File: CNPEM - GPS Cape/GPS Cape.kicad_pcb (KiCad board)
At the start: 2 copper layers, 11 parts, among them J101 Adafruit_ultimate_GPS_breakout, U101 74LS123

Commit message: schematics and pcb finished
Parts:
- added C104: 100n, Capacitors_SMD:C_0805_HandSoldering, F.Cu at (172.1, 94.0)
- added C105: 100n, Capacitors_SMD:C_0805_HandSoldering, F.Cu at (143.5, 99.1)
- added C106: 0.1u, Capacitors_SMD:C_0805_HandSoldering, B.Cu at (132.7, 96.5)
- added R103: 10k, Resistors_SMD:R_0805_HandSoldering, F.Cu at (149.9, 116.2)
- added R104: 10k, Resistors_SMD:R_0805_HandSoldering, B.Cu at (132.7, 101.0)
- moved D101 10.5 mm to (144.8, 116.2), turned to 270 degrees
- moved C103 8.98 mm to (151.8, 111.1)
- moved JP102 8.89 mm to (164.5, 87.0)
- moved JP101 8.25 mm to (159.4, 87.0)
- moved R102 6.35 mm to (147.3, 105.4), turned to 90 degrees
- moved C102 3.42 mm to (154.9, 116.2)
- moved C101 2.54 mm to (151.8, 99.1), turned to 0 degrees
- moved R101 1.80 mm to (154.9, 105.4)
- moved Beagle101 0.25 mm to (148.6, 104.8)
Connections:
- Beagle101 pad B1: (no net) -> GND
- Beagle101 pad B10: (no net) -> Net-(Beagle101-PadB10)
- Beagle101 pad B11: (no net) -> Net-(Beagle101-PadB11)
- Beagle101 pad B12: (no net) -> Net-(Beagle101-PadB12)
- Beagle101 pad B13: (no net) -> Net-(Beagle101-PadB13)
- Beagle101 pad B14: (no net) -> Net-(Beagle101-PadB14)
- Beagle101 pad B15: (no net) -> Net-(Beagle101-PadB15)
- Beagle101 pad B16: (no net) -> Net-(Beagle101-PadB16)
- Beagle101 pad B17: (no net) -> Net-(Beagle101-PadB17)
- Beagle101 pad B18: (no net) -> Net-(Beagle101-PadB18)
- Beagle101 pad B19: (no net) -> Net-(Beagle101-PadB19)
- Beagle101 pad B2: (no net) -> Net-(Beagle101-PadB2)
- Beagle101 pad B20: (no net) -> Net-(Beagle101-PadB20)
- Beagle101 pad B21: (no net) -> Net-(Beagle101-PadB21)
- Beagle101 pad B22: (no net) -> Net-(Beagle101-PadB22)
- Beagle101 pad B23: (no net) -> Net-(Beagle101-PadB23)
- Beagle101 pad B24: (no net) -> Net-(Beagle101-PadB24)
- Beagle101 pad B25: (no net) -> Net-(Beagle101-PadB25)
- Beagle101 pad B26: (no net) -> Net-(Beagle101-PadB26)
- Beagle101 pad B27: (no net) -> Net-(Beagle101-PadB27)
- Beagle101 pad B28: (no net) -> Net-(Beagle101-PadB28)
- Beagle101 pad B29: (no net) -> Net-(Beagle101-PadB29)
- Beagle101 pad B3: (no net) -> Net-(Beagle101-PadB3)
- Beagle101 pad B30: (no net) -> Net-(Beagle101-PadB30)
- Beagle101 pad B31: (no net) -> Net-(Beagle101-PadB31)
- Beagle101 pad B32: (no net) -> Net-(Beagle101-PadB32)
- Beagle101 pad B33: (no net) -> Net-(Beagle101-PadB33)
- Beagle101 pad B34: (no net) -> Net-(Beagle101-PadB34)
- Beagle101 pad B35: (no net) -> Net-(Beagle101-PadB35)
- Beagle101 pad B36: (no net) -> Net-(Beagle101-PadB36)
- Beagle101 pad B37: (no net) -> Net-(Beagle101-PadB37)
- Beagle101 pad B38: (no net) -> Net-(Beagle101-PadB38)
- Beagle101 pad B39: (no net) -> Net-(Beagle101-PadB39)
- Beagle101 pad B4: (no net) -> Net-(Beagle101-PadB4)
- Beagle101 pad B40: (no net) -> Net-(Beagle101-PadB40)
- Beagle101 pad B41: (no net) -> Net-(Beagle101-PadB41)
- Beagle101 pad B42: (no net) -> Net-(Beagle101-PadB42)
- Beagle101 pad B43: (no net) -> Net-(Beagle101-PadB43)
- Beagle101 pad B44: (no net) -> Net-(Beagle101-PadB44)
- Beagle101 pad B45: (no net) -> Net-(Beagle101-PadB45)
- Beagle101 pad B46: (no net) -> Net-(Beagle101-PadB46)
- Beagle101 pad B5: (no net) -> Net-(Beagle101-PadB5)
- Beagle101 pad B6: (no net) -> Net-(Beagle101-PadB6)
- Beagle101 pad B7: (no net) -> Net-(Beagle101-PadB7)
- Beagle101 pad B8: (no net) -> Net-(Beagle101-PadB8)
- Beagle101 pad B9: (no net) -> Net-(Beagle101-PadB9)
- Beagle101 pad C4: +3V3 -> VCC
- Beagle101 pad C44: Net-(Beagle101-PadC44) -> GND
- C102 pad 2: +3V3 -> Net-(C102-Pad2)
- D101 pad 2: +3V3 -> VCC
- J101 pad 2: +3V3 -> Net-(C106-Pad2)
- J101 pad 8: +3V3 -> VCC
- R101 pad 1: +3V3 -> VCC
- U101 pad 16: +3V3 -> VCC
- U101 pad 3: +3V3 -> Net-(C102-Pad2)
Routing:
- net VCC: track 0.00 -> 97.4 mm
- net +3V3: track 47.1 -> 0.00 mm
- net /TX_GPS: track 0.00 -> 36.4 mm
- net GND: track 95.2 -> 128.3 mm
- net /RX_GPS: track 0.00 -> 32.9 mm
- net Net-(C101-Pad1): track 5.47 -> 32.1 mm
- net Net-(C102-Pad2): track 0.00 -> 22.0 mm
- net Net-(C106-Pad2): track 0.00 -> 19.7 mm
- net /PPS_ENL: track 28.8 -> 18.6 mm
- net Net-(C103-Pad1): track 8.08 -> 16.1 mm
- net Net-(D101-Pad1): track 3.32 -> 9.45 mm
- net /PPS: track 30.2 -> 35.6 mm
- net Net-(Beagle101-PadC12): track 10.8 -> 10.2 mm
- added copper zone on B.Cu, net GND
- added copper zone on F.Cu, net GND
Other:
- board outline added: 87 x 54.6 mm

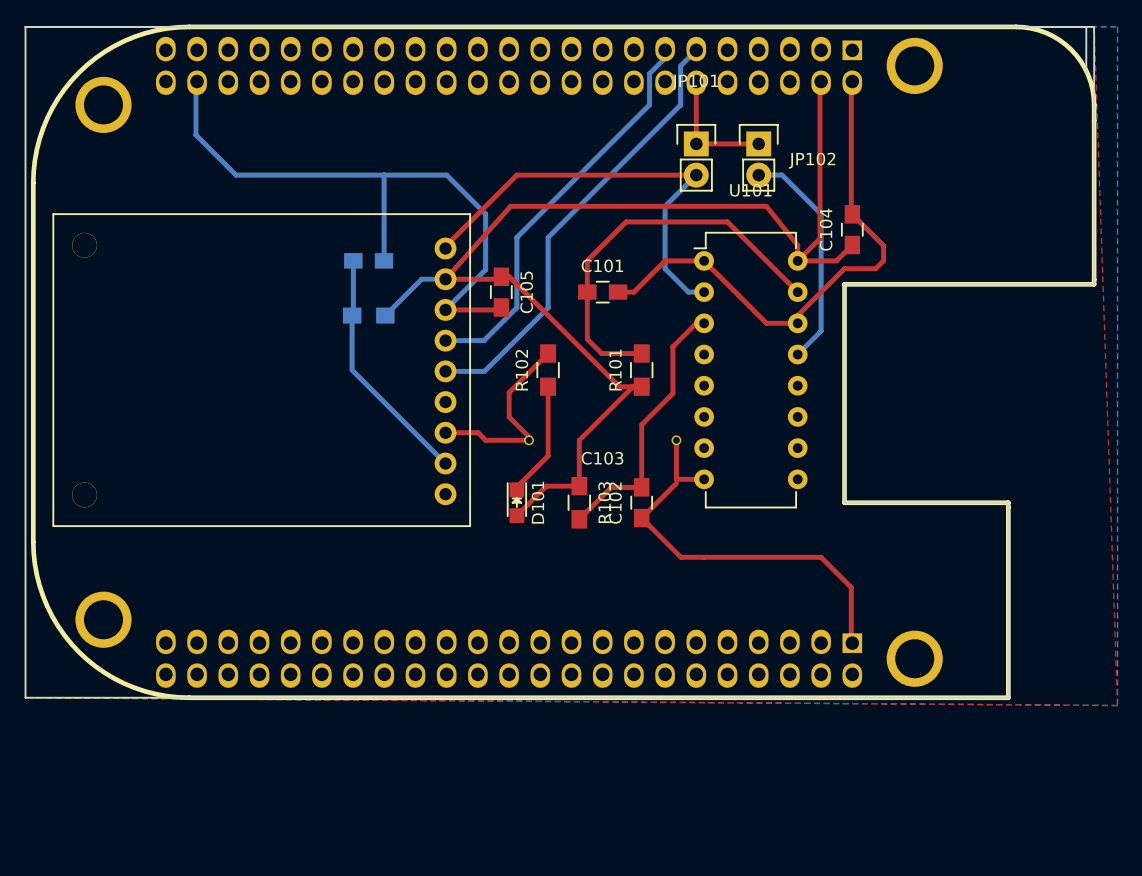
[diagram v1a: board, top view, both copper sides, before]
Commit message: bbb pins connections put in bottom layer and logo inserted
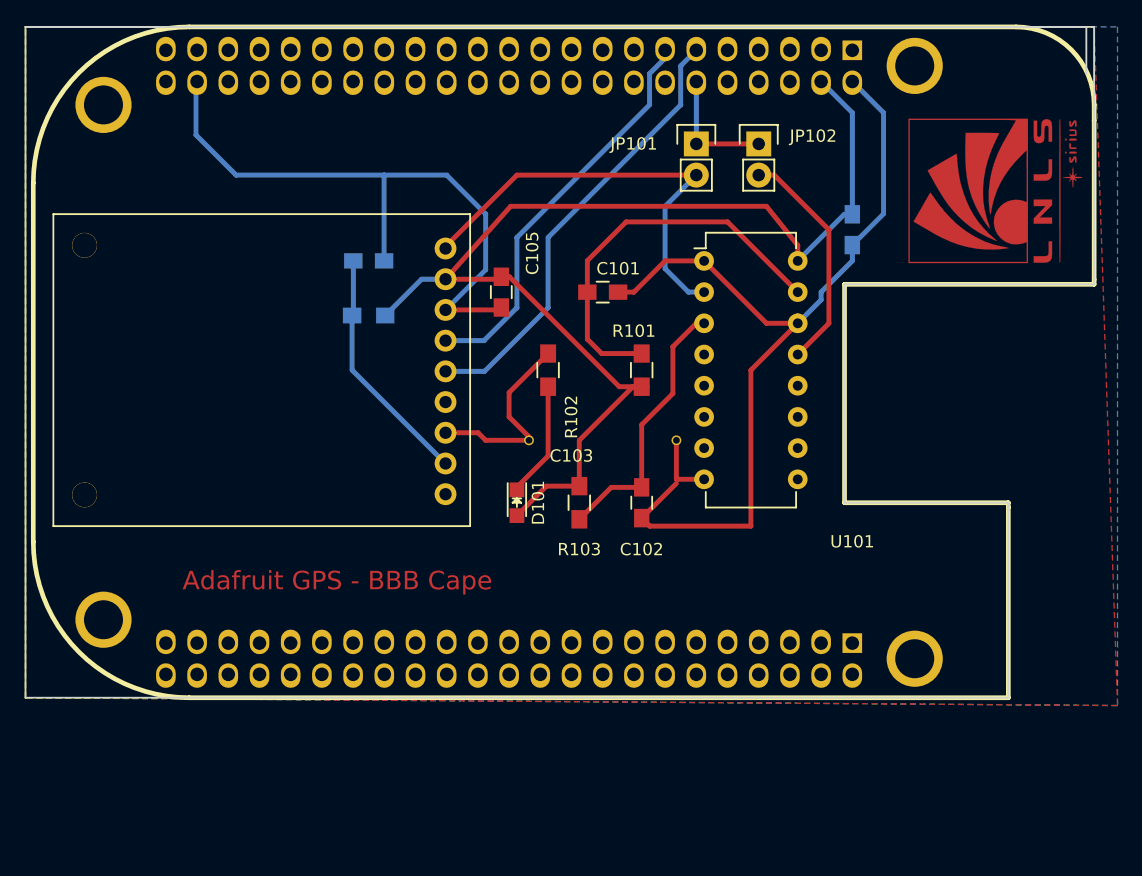
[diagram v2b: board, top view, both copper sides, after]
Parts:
- added G***: LOGO, Controle:LNLS_Conversor_USB_RS485, F.Cu at (183.5, 90.8)
- C104: moved to B.Cu
- turned C104 to 270 degrees
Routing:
- net GND: track 128.3 -> 130.7 mm
- net VCC: track 97.4 -> 95.8 mm
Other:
- board text added: "Adafruit GPS - BBB Cape"

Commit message: LED and components revised
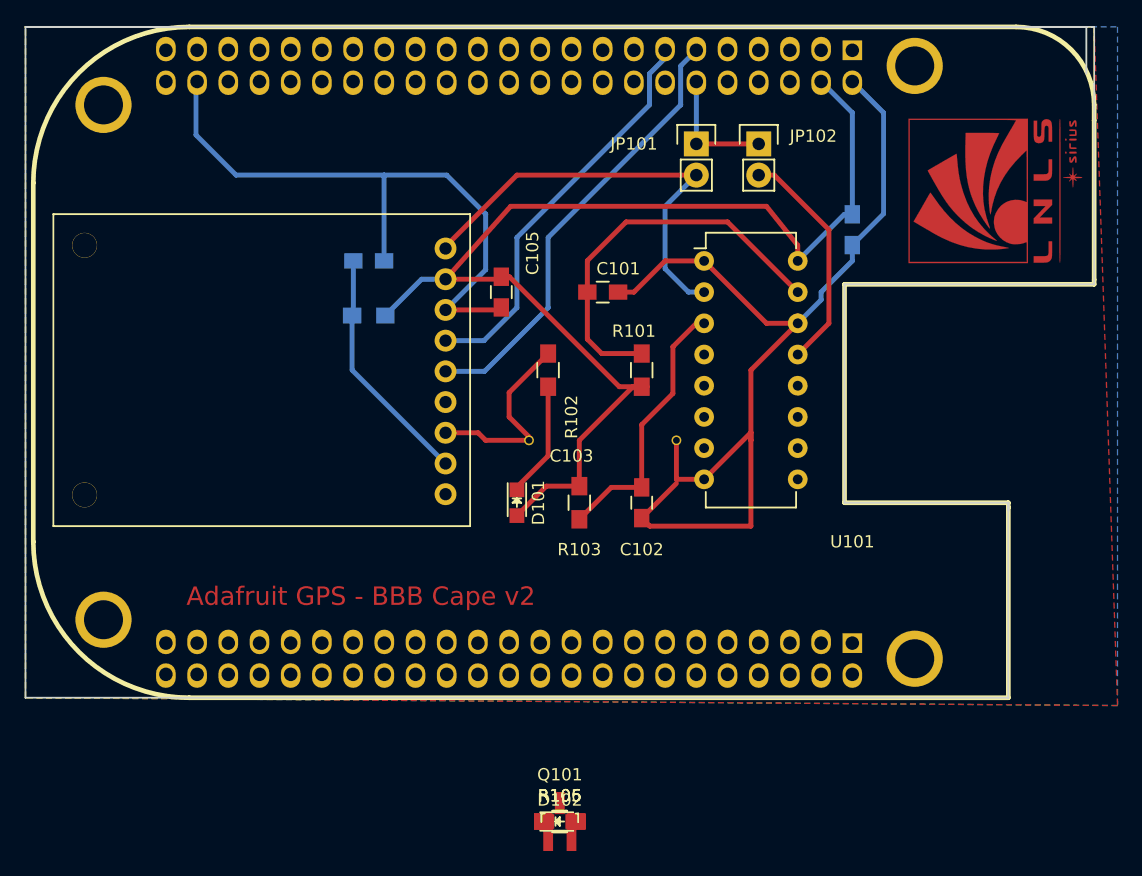
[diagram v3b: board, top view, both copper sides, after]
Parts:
- added D102: LED, LEDs:LED_0805, F.Cu at (148.3, 142.2)
- added Q101: Q_NPN_BEC, TO_SOT_Packages_SMD:SOT-23_Handsoldering, F.Cu at (148.3, 142.2)
- added R105: 10k, Resistors_SMD:R_0805_HandSoldering, F.Cu at (148.3, 142.2)
- added R106: 100, Resistors_SMD:R_0805_HandSoldering, F.Cu at (148.3, 142.2)
- C101: value 10n -> 1u
- R101: value 200K -> 1M
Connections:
- Beagle101 pad B1: GND -> Net-(Beagle101-PadB1)
- Beagle101 pad C44: GND -> Net-(Beagle101-PadC44)
- Beagle101 pad C6: Net-(Beagle101-PadC6) -> +5V
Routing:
- net Net-(Beagle101-PadC44): track 0.00 -> 4.13 mm
- net GND: track 130.7 -> 132.3 mm
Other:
- board text added: "Adafruit GPS - BBB Cape v2"
- board text removed: "Adafruit GPS - BBB Cape"
